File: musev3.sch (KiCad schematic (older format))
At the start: 9 parts

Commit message: Completed rev 3.00
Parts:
- removed R?: 3k, symbol R
- removed R?: 1k, symbol R
- removed SW?: RST_BTN, symbol DPST
- added ANT?: ANT-2.4-CHP, symbol ANT-2.4-CHP
- added C?: 1uF, symbol CP1
- added C?: 100nF, symbol C
- added C? (x4): 4.7uF, symbol CP1
- added C?: 0.1uF, symbol C-RESCUE-museV2
- added C? (x4): 0.1uF, symbol C
- added C? (x3): 10uF, symbol CP1
- added C? (x3): 47uF, symbol CP1
- added CON? (x2): RCA_conn_x2, symbol RCA_conn_x2
- added CON? (x2): 3.5mm_conn_tip_switch, symbol 3.5mm_conn_tip_switch
- added D?: PWR_LED, symbol LED
- added P?: RF_DEBUG_CONN, symbol CONN_02X05
- added P?: UART_CONN, symbol CONN_01X06
- added P?: PWR_CONN, symbol CONN_01X03
- added P?: LED_CONN, symbol CONN_01X10
- added R?: 200k, symbol R
- added R? (x22): 4.7k, symbol R
- added SW? (x2): DUAL_SWITCH_INV, symbol DUAL_SWITCH_INV
- added SW?: SPST, symbol SPST
- added U?: RFM12B, symbol RFM12B
- added U?: R1171S331B, symbol R1171S331B
- added U?: GTL2010, symbol GTL2010
- added U?: PCM3060, symbol PCM3060
- added U?: CFPS-73 - 24.567MHz, symbol CFPS-73
- added U? (x4): 74HC04, symbol 74HC04
- added U?: LM2662, symbol LM2662
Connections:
- net labels added: +5V, ADC_VINL, ADC_VINR, ADC_VOUTL+, ADC_VOUTL-, ADC_VOUTR+, ADC_VOUTR-, AUDIO_IN_L, AUDIO_IN_R, AUDIO_OUT_L, AUDIO_OUT_R, CLK_OUT, I2C_SCL, I2C_SDA, I2S_CLK, I2S_SDI, I2S_SDO, I2S_SLK, I2S_WS, IA_LED_0(3.3), IA_LED_0(5), IA_LED_1(3.3), IA_LED_1(5), IA_LED_2(3.3), IA_LED_2(5), IA_LED_3(3.3), IA_LED_3(5), IA_LED_4(3.3), IA_LED_4(5), IA_LED_5(3.3), IA_LED_5(5), IA_LED_6, IA_LED_6(5), IA_LED_7, IA_LED_7(5), IA_LED_8(3.3), IA_LED_8(5), IA_LED_9(3.3), IA_LED_9(5), ONION_RST, PSU_CTL, RF_RST, RX/IA_LED_6, RX/IA_LED_6(3.3), SPI_CLK, SPI_CS, SPI_MISO, SPI_MOSI, SYS_CLK, TX/IA_LED_7, TX/IA_LED_7(3.3), UART_RX, UART_TX, nINT/VDI, nIRQ, ~CODEC_RST, ~RF_RST
- net labels removed: RST_BTN
- wire segments 38 -> 300
- no-connect marks 7 -> 15
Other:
- note added: "4.7uF electrolytic capacitors recommended\nfor 3Hz cutoff frequency"
- note added: "Are more power inputs required?\nHow is the relay wired? Do we have a standby PSU?"
- note added: "Audio CODEC"
- note added: "Audio Input/Output Buffers"
- note added: "Audio Input/Output Jacks"
- note added: "FC = V+ for \n150kHz F_OSC"
- note added: "FM Radio"
- note added: "FM Radio Pin Breakout"
- note added: "Hardware designs by Jason Merlo"
- note added: "LED Level Shifter"
- note added: "LED Pin Breakout"
- note added: "LV = GND for\nV+ > 3.5V"
- note added: "Low Drop-Out Regulator"
- note added: "MODE -> LOW = I2C\nADR -> LOW = 0x8C"
- note added: "Max load capacitance 50pF"
- note added: "Microcontroller"
- note added: "NOTE: Capacitors must have ESR < 0.2 Ohm"
- note added: "Not sure\nof this"
- note added: "Onion UART"
- note added: "PSU Input"
- note added: "Power LED"
- note added: "REMEMBER I2C/SPI BUS TERMINATION"
- note added: "RF & CODEC reset are active low\nOnion reset is active high (DOUBLE CHECK)"
- note added: "System Clock Generator\n(Audio)"
- note added: "UART Debug Switch"
- note added: "Voltage Inverter"
- note added: "Will likely change to custom connectors"
- note added: "nSEL must be toggled\nbetween control words"
- note removed: "Decouping Capacitors"
- moved on the sheet: C?, J?, JP?, U?

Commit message: Updated to rev 3.1
Changed radio to RFM69HCW
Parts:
- removed P?: RF_DEBUG_CONN, symbol CONN_02X05
- removed U?: RFM12B, symbol RFM12B
- added P?: RF_DEBUG, symbol CONN_01X06
- added U?: RFM69HCW, symbol RFM69HCW
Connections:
- net labels added: RF_DIO0, RF_DIO3, RF_DIO4, RF_DIO5
- net labels removed: CLK_OUT, nINT/VDI, nIRQ
- wire segments 300 -> 375
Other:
- note added: "DIO Rx - MODE: Continous 00\n0 -> SyncAddress\n1 -> DCLK\n2 -> DATA\n3 -> RSSI\n4 -> Timeout\n5 -> CLKOUT"
- note removed: "Not sure\nof this"
- note removed: "nSEL must be toggled\nbetween control words"
- moved on the sheet: ANT?, C?

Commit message: Added annotations, fixed ERC errors
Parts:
- removed P?: PWR_CONN, symbol CONN_01X03
- removed SW?: SPST, symbol SPST
- added P1: PWR_IN_PINS, symbol PWR_IN_PINS
- added SW2: DPST, symbol DPST
- added unit 2 of U1
- gave numbers to parts that had none: 62
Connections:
- net I2S_SLK is gone; now on net I2S_CLK: U4.3 (GPIO_3/I2S_CLK)
- net VCC is gone; now on net +3.3V: U1.14 (VCC), U1.14 (VCC), U1.14 (VCC), U1.14 (VCC)
- net +3.3V: now also SW2.1, SW2.3, U1.14 (VCC)
- net +5V: now also P1.2 (P2)
- net GND: now also CON3.1, P1.1 (P1), U1.7 (GND)
- net ONION_RST: now also U1.10; no longer U1.8
- net PSU_CTL: now also P1.3 (P3)
- net RF_RST: now also U1.4
- net RX/IA_LED_6: now also U4.28 (GPIO_13/RX0)
- net TX/IA_LED_7: now also U4.27 (GPIO_12/TX0)
- net ~CODEC_RST: now also U1.6; no longer U1.4
- net at R2.2, U1.1: now also U1.5, U1.9, SW2.2, SW2.4; no longer U1.3, U1.5
- net -5V: now reaches C18.1, U5.5 (OUT)
- net IA_LED_6 renamed IA_LED_6(3.3)
- net IA_LED_6(3.3): now also R10.1, U3.9 (S7)
- net IA_LED_7 renamed IA_LED_7(3.3)
- net IA_LED_7(3.3): now also R11.1, U3.10 (S8)
- removed net RX/IA_LED_6(3.3): R10.1, U3.9 (S7), U4.28 (GPIO_13/RX0)
- removed net TX/IA_LED_7(3.3): R11.1, U3.10 (S8), U4.27 (GPIO_12/TX0)
- net ~RF_RST: no longer names the net of U1.2
- net ~RF_RST: now also U1.3
- new net: U1.11, U1.8
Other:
- note added: "CODEC reset active low\nRF & Onion reset active high (DOUBLE CHECK)"
- note removed: "RF & CODEC reset are active low\nOnion reset is active high (DOUBLE CHECK)"
- moved on the sheet: R2, U1A

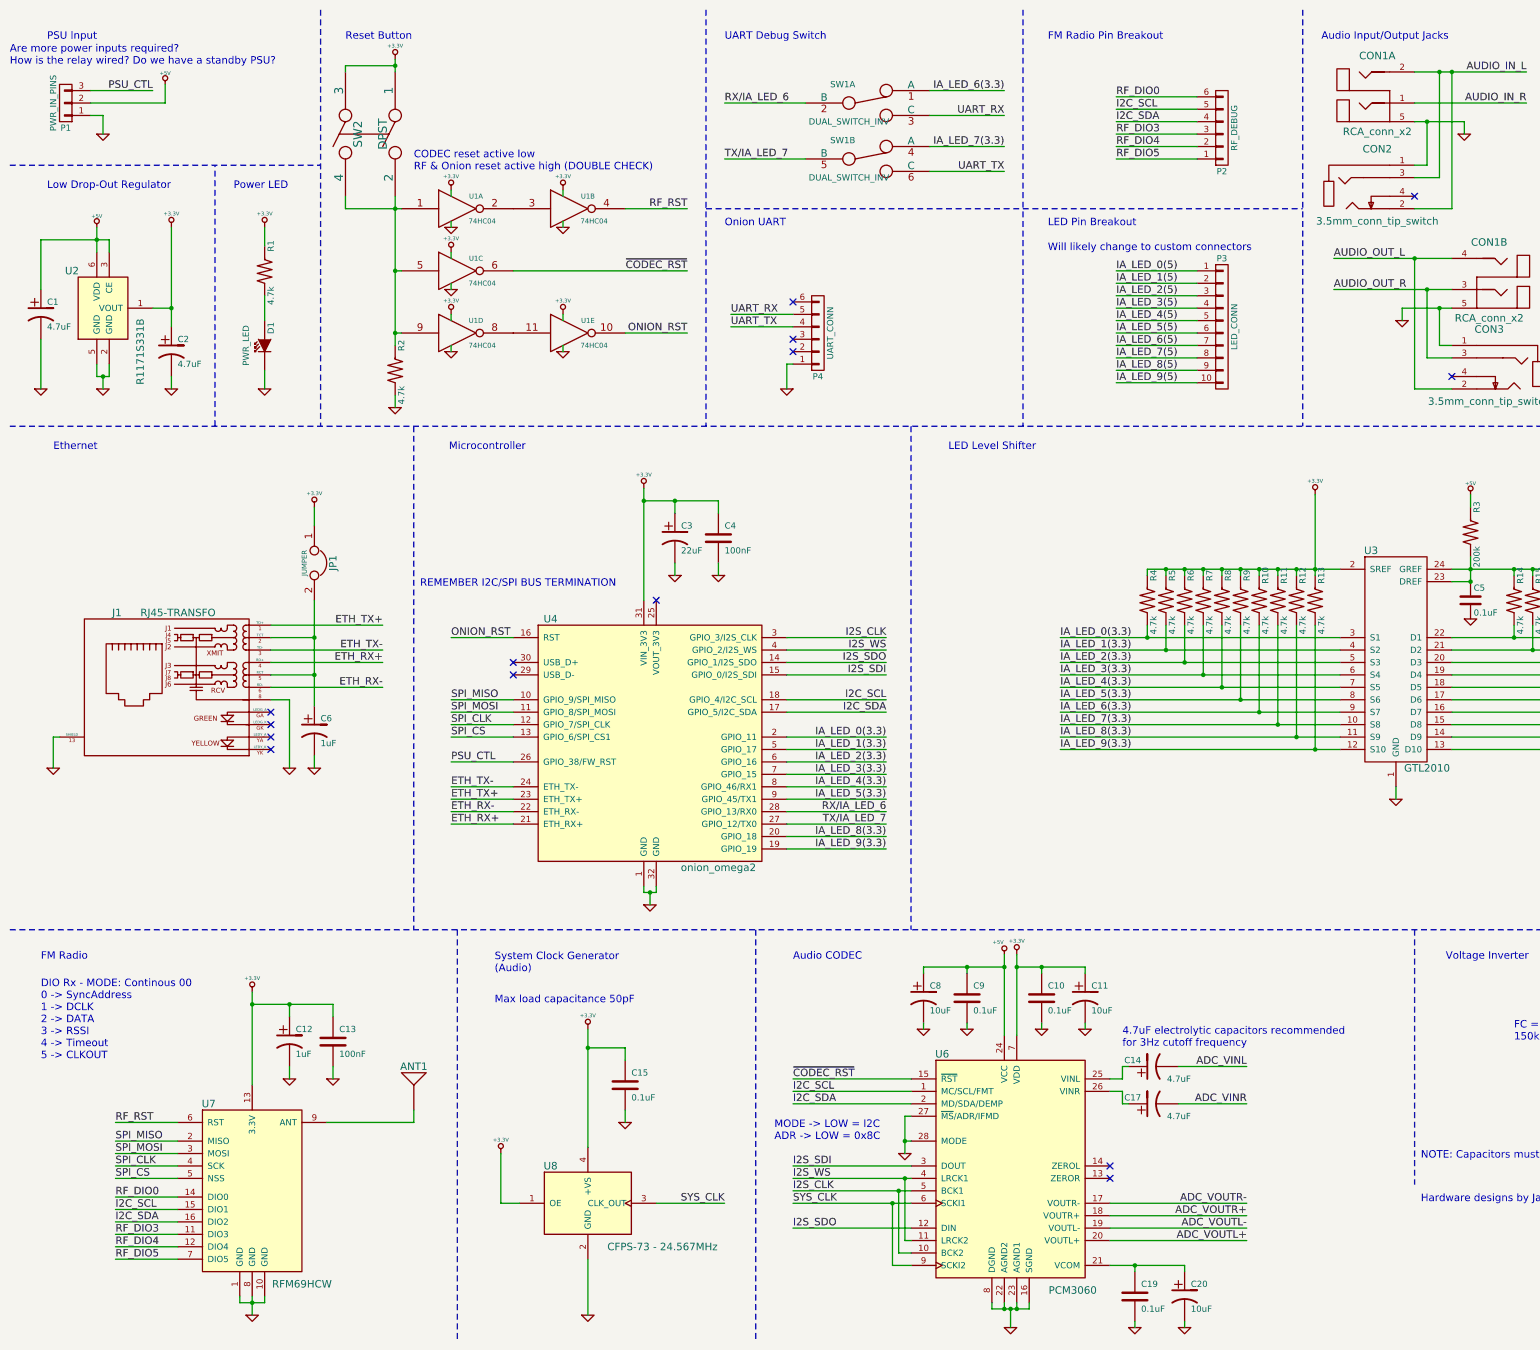
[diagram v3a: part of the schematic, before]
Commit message: Changed CODED to SPI to remove the need for i2c bus
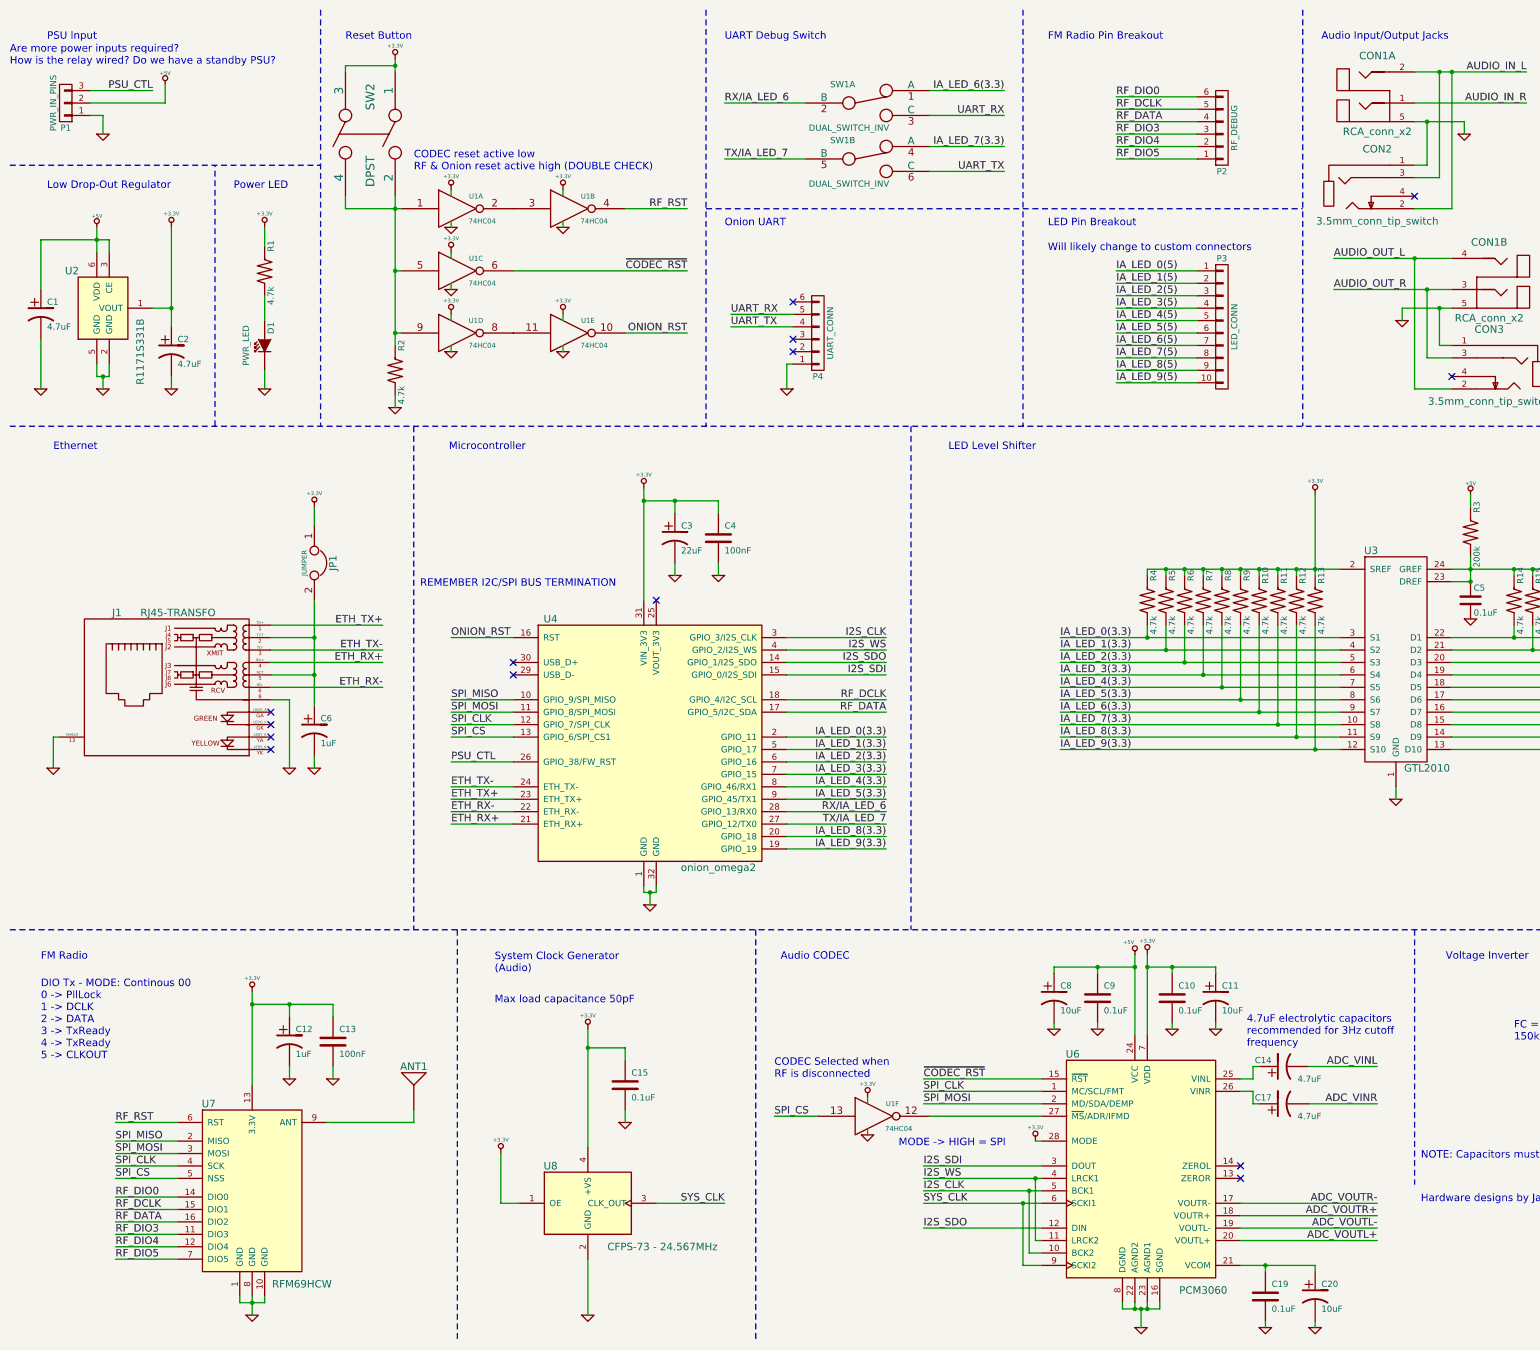
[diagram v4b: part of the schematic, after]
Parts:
- added unit 6 of U1
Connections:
- net +3.3V: now also U6.28 (MODE), U1.14 (VCC)
- net GND: now also U1.7 (GND); no longer U6.27 (~MS~/ADR/IFMD), U6.28 (MODE)
- net SPI_CLK: now also U6.1 (MC/SCL/FMT)
- net SPI_CS: now also U1.13
- net SPI_MOSI: now also U6.2 (MD/SDA/DEMP)
- net I2C_SCL renamed RF_DCLK
- net RF_DCLK: no longer U6.1 (MC/SCL/FMT)
- net I2C_SDA renamed RF_DATA
- net RF_DATA: no longer U6.2 (MD/SDA/DEMP)
- new net: U1.12, U6.27 (~MS~/ADR/IFMD)
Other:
- note added: "4.7uF electrolytic capacitors \nrecommended for 3Hz cutoff \nfrequency"
- note added: "CODEC Selected when \nRF is disconnected"
- note added: "DIO Tx - MODE: Continous 00\n0 -> PllLock\n1 -> DCLK\n2 -> DATA\n3 -> TxReady\n4 -> TxReady\n5 -> CLKOUT"
- note added: "MODE -> HIGH = SPI"
- note removed: "4.7uF electrolytic capacitors recommended\nfor 3Hz cutoff frequency"
- note removed: "DIO Rx - MODE: Continous 00\n0 -> SyncAddress\n1 -> DCLK\n2 -> DATA\n3 -> RSSI\n4 -> Timeout\n5 -> CLKOUT"
- note removed: "MODE -> LOW = I2C\nADR -> LOW = 0x8C"
- moved on the sheet: C10, C11, C14, C17, C19, C20, C8, C9, U6

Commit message: Updated decoupling capacitors for op-amp output
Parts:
- removed ANT1: ANT-2.4-CHP, symbol ANT-2.4-CHP
- added C1, C3, C5, C7: 10uF, symbol CP1
- added C2, C4, C6, C8: 100nF, symbol C
- added P5: SMA, symbol BNC
- renumbered C2 to C10, C3 to C11, C4 to C12, C5 to C13, C6 to C14, C7 to C15, C8 to C16, C9 to C17, C10 to C18, C11 to C19, C12 to C20, C13 to C21, C14 to C22, C15 to C23, C16 to C24, C17 to C25, C18 to C26, C19 to C27, C20 to C28, C1 to C9
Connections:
- net +5V: now also C1.1, C2.1, C3.1, C4.1
- net -5V: now also C5.2, C6.1, C7.2, C8.1
- net GND: now also C1.2, C2.2, C3.2, C4.2, C5.1, C6.2, C7.1, C8.2, P5.2 (Ext)
- net at U7.9 (ANT): now also P5.1 (In)
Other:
- note added: "10uF = Tantalum\n100nF = Ceramic X7R"
- note removed: "REMEMBER I2C/SPI BUS TERMINATION"
- moved on the sheet: C13, R10, R11, R12, R13, R14, R15, R16, R17, R18, R19, R20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

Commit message: Added EMI and ESD protection to audio interface, started assoc. footprints
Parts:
- added C41, C42, C43, C44: 100nF, Capacitors_SMD:C_1206_HandSoldering, symbol C
- added C45, C46, C47, C48: 5000pF, Capacitors_SMD:C_1206_HandSoldering, symbol C
- added D6, D7: TPD2E1B06, symbol TPD2E1B06
- C1, C10, C3, C5, C7, C9: footprint (none) -> Capacitors_SMD:C_0805_HandSoldering
- C2, C4, C6, C8: value 100nF -> 0.1uF; footprint (none) -> Capacitors_SMD:C_1206_HandSoldering
- SW1: value DUAL_SWITCH_INV -> UART_DEBUG
- SW2: value DPST -> RST
- renumbered U8 to X1
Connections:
- net +5V: now also C41.1, C42.1
- net -5V: now also C43.1, C44.1
- net AUDIO_IN_L: now also C46.1, D6.2; no longer CON2.3
- net AUDIO_IN_R: now also CON2.3, C45.1, D6.1
- net AUDIO_OUT_L: now also C47.1, D7.1
- net AUDIO_OUT_R: now also C48.1, D7.2
- net GND: now also C41.2, C42.2, C43.2, C44.2, C45.2, C46.2, C47.2, C48.2, D6.4, D6.5, D7.4, D7.5
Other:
- note added: "10uF = Tantalum\n100nF,0.1uF = Ceramic X7R"
- note added: "Refer to datasheet\nfor TVS layout"
- note added: "Will likely change to \ncustom connectors"
- note removed: "10uF = Tantalum\n100nF = Ceramic X7R"
- note removed: "Will likely change to custom connectors"
- moved on the sheet: C3, C4, C7, C8, CON1A, CON2, CON3, P2, P3, P4
